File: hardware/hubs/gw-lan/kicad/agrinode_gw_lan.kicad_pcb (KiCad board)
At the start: 2 copper layers, 150 x 96 mm, 126 parts, among them J1 DC 12V 5.5/2.1, J10 LAN, J2 DC IN 7-24V, J3 SOLAR 6-24V, J4 USB 5V / PROG, J5 BAT NTC 10k, J6 PROG, J7 I2C, J8 LED STRIP WS2813, J9 RS-485, Q1 AO3401A, Q2 AO3401A, Q3 MMBT3904, Q4 MMBT3904, Q5 BSS138, Q6 MMBT3904, SW1 RESET, SW2 BOOT / PAIR, U1 LM2596S-5.0, U2 TP4056, U3 MIC29302WU, U4 ESP32-WROOM-32E-N8, U5 CH340C, U6 DS3231MZ, U7 MAX3485ESA, U8 Ra-02 SX1278 433MHz, U9 ENC28J60-I/SO, Y1 25MHz

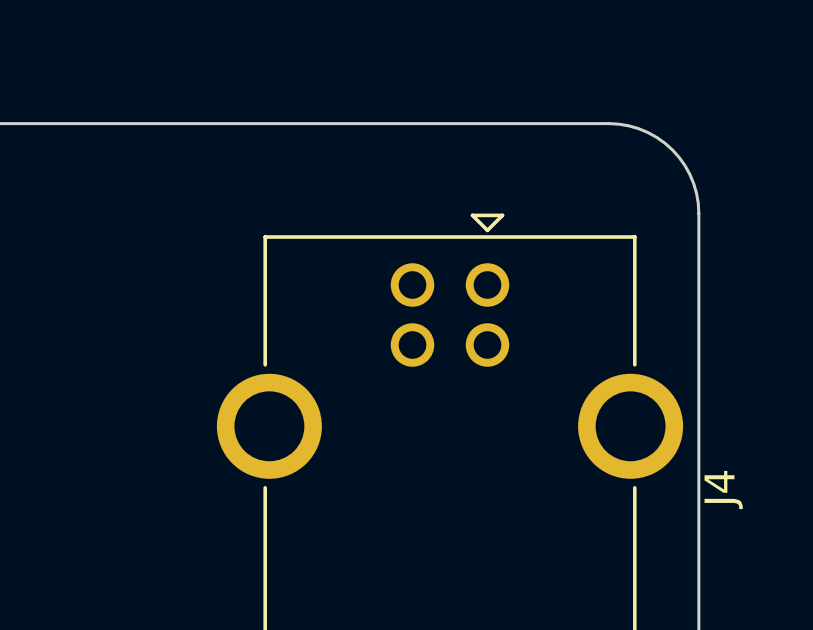
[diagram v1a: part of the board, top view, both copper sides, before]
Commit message: hubs: boards after GPIO remap (placement; routing in progress)
Co-Authored-By: Claude Opus 5.5 <noreply@anthropic.com>
Claude-Session: https://claude.ai/code/session_014J7amXZ5Y6AZWEh5CjDNja
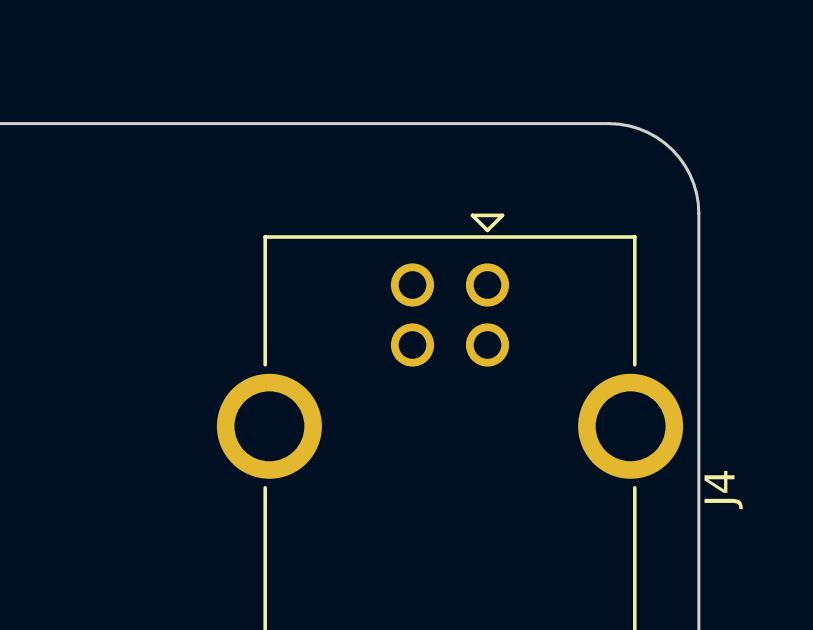
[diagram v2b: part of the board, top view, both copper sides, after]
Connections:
- U4 pad 10: RS485_DE -> unconnected-(U4-IO25-Pad10)
- U4 pad 11: LORA_DIO0 -> unconnected-(U4-IO26-Pad11)
- U4 pad 14: CHRG_N -> unconnected-(U4-IO12-Pad14)
- U4 pad 16: unconnected-(U4-IO13-Pad16) -> CHRG_N
- U4 pad 26: ETH_CS -> RS485_DE
- U4 pad 27: unconnected-(U4-IO16-Pad27) -> RS485_RX
- U4 pad 28: unconnected-(U4-IO17-Pad28) -> RS485_TX
- U4 pad 33: /ESP32, programming, buttons, RTC, LED strip, buzzer/I2C_SDA -> LORA_DIO0
- U4 pad 36: /ESP32, programming, buttons, RTC, LED strip, buzzer/I2C_SCL -> ETH_CS
- U4 pad 8: RS485_TX -> /ESP32, programming, buttons, RTC, LED strip, buzzer/I2C_SCL
- U4 pad 9: RS485_RX -> /ESP32, programming, buttons, RTC, LED strip, buzzer/I2C_SDA

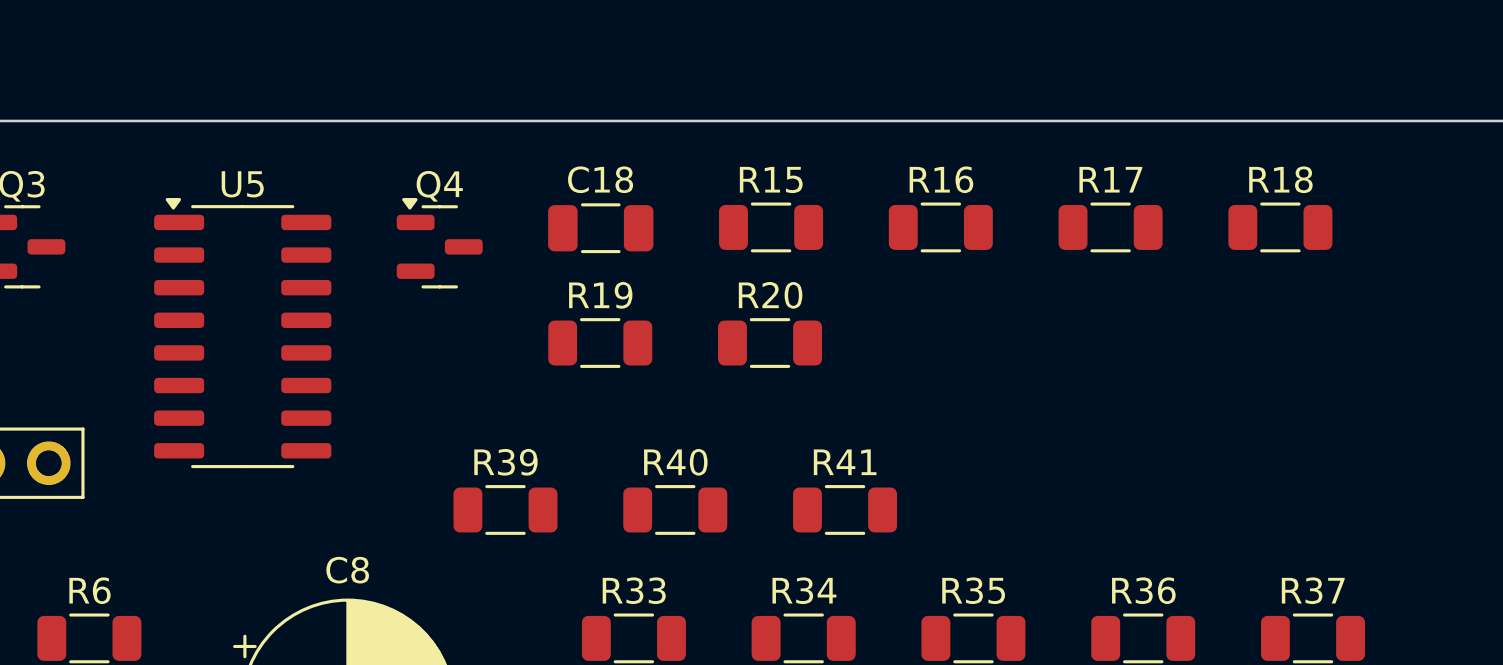
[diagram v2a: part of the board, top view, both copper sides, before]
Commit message: hubs: CH340C rotated so USB D+/D- face the USB-B jack; reroute in progress
Co-Authored-By: Claude Opus 5.5 <noreply@anthropic.com>
Claude-Session: https://claude.ai/code/session_014J7amXZ5Y6AZWEh5CjDNja
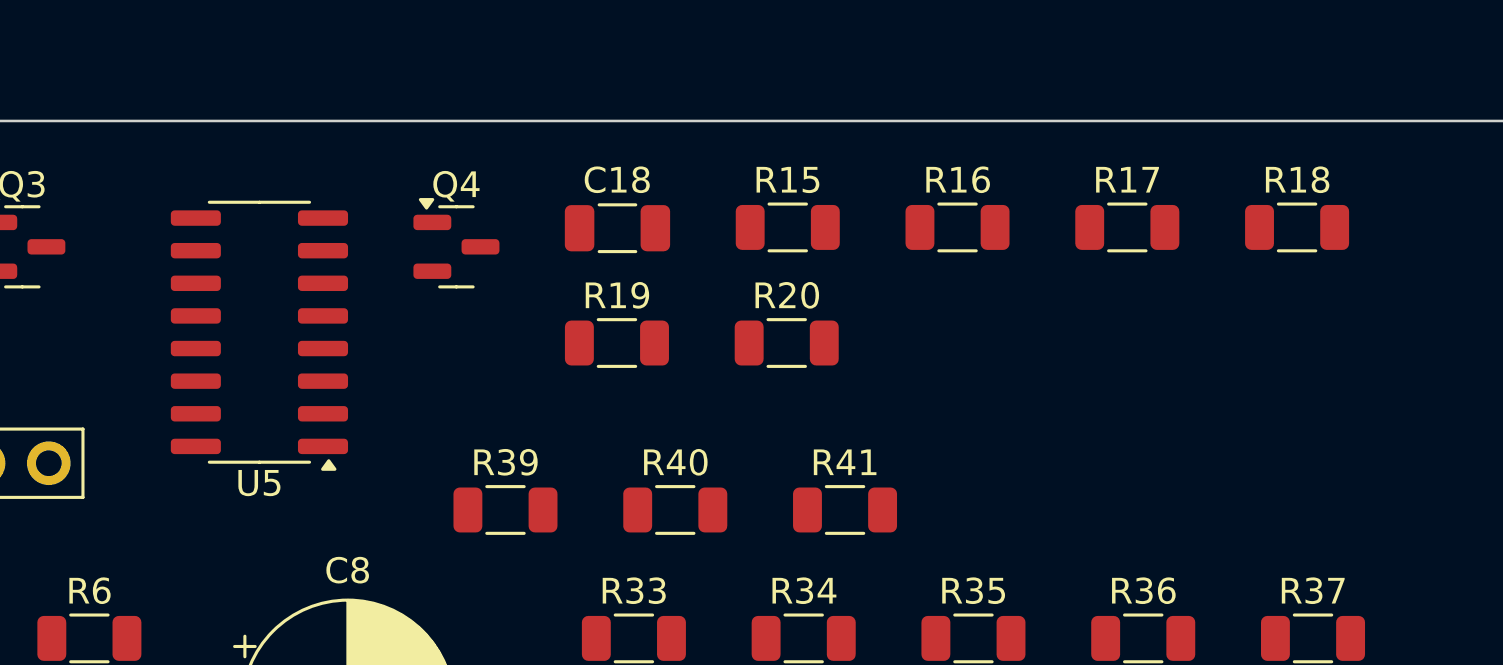
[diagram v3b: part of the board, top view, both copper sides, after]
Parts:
- moved U5 0.67 mm to (133.7, 58.2), turned to 180 degrees
- moved C18 0.65 mm to (147.7, 54.2)
- moved Q4 0.65 mm to (141.4, 54.9)
- moved R16 0.65 mm to (160.9, 54.1)
- moved R18 0.65 mm to (174.1, 54.1)
- moved R19 0.65 mm to (147.6, 58.6)
- moved R20 0.65 mm to (154.3, 58.6)
- moved R15 0.65 mm to (154.3, 54.1)
- moved R17 0.65 mm to (167.5, 54.1)

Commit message: hubs: routing progress snapshot
Co-Authored-By: Claude Opus 5.5 <noreply@anthropic.com>
Claude-Session: https://claude.ai/code/session_014J7amXZ5Y6AZWEh5CjDNja
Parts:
- moved C10 165.3 mm to (0.00, 0.00)
- moved U6 28.2 mm to (137.7, 95.7), turned to 180 degrees
- moved R22 21.9 mm to (137.6, 102.1)
- moved R21 11.0 mm to (136.4, 89.6)
- moved R28 2.73 mm to (145.8, 101.1)
- moved D10 1.40 mm to (145.4, 95.9)
